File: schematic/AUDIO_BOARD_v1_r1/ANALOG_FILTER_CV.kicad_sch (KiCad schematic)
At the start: 23 parts, among them U4 LM13700, U5 OPA1678, U6 4053, U7 DAC8565, U8 LM13700

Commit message: render!
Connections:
- net at R21.2, R23.1, U5.2 (-): now also R20.2
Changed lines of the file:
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@@
+		)
+	)
+	(wire
+		(pts
+			(xy 55.88 124.46) (xy 55.88 139.7)
+		)
+		(stroke
+			(width 0)
+			(type default)
 		)
 	)

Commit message: more audio board placement
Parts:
- added C90, C91, C92, C93, C94, C95: 100nF, Capacitor_SMD:C_0402_1005Metric, symbol Device:C_Small
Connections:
- net +5V: now also C90.1, C92.1, C94.1
- net -5V: now also C91.1, C93.1, C95.1
- net GND: now also C90.2, C91.2, C92.2, C93.2, C94.2, C95.2
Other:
- note added: "DECOUPLING 100nF/IC (U4/U8/U5/U6 rails +/-5V ; U7 DAC +5V)"

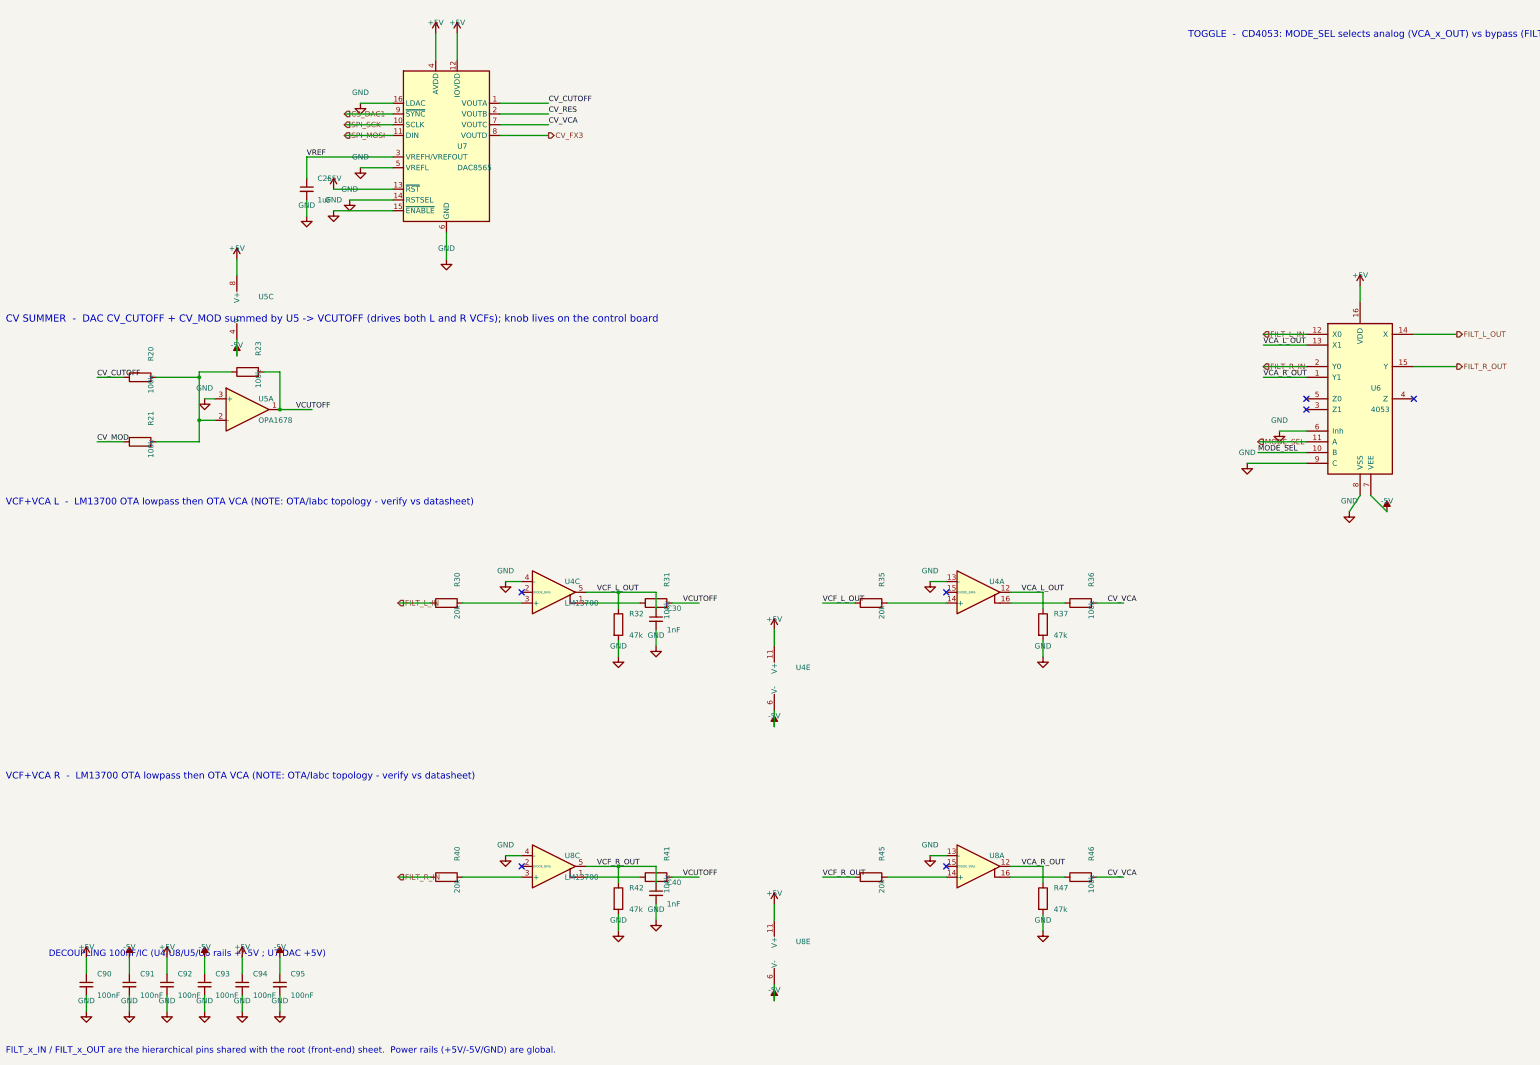
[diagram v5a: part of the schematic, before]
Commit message: placement. start with each sheet for the most part
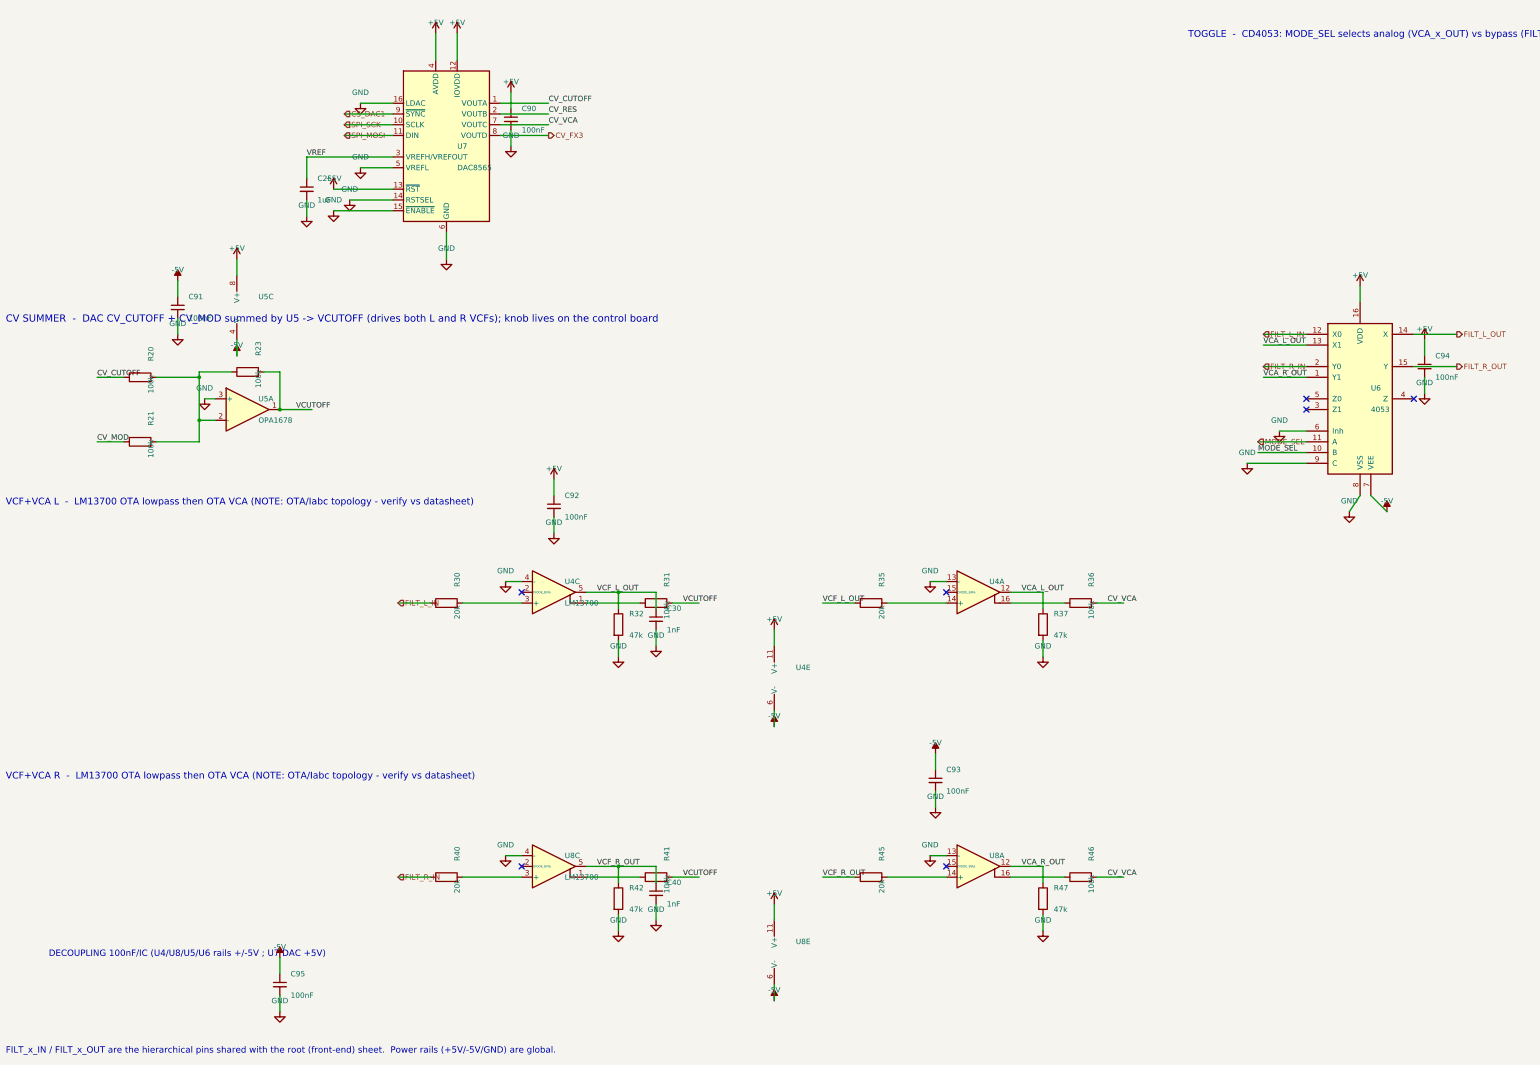
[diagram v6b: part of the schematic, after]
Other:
- moved on the sheet: C90, C91, C92, C93, C94

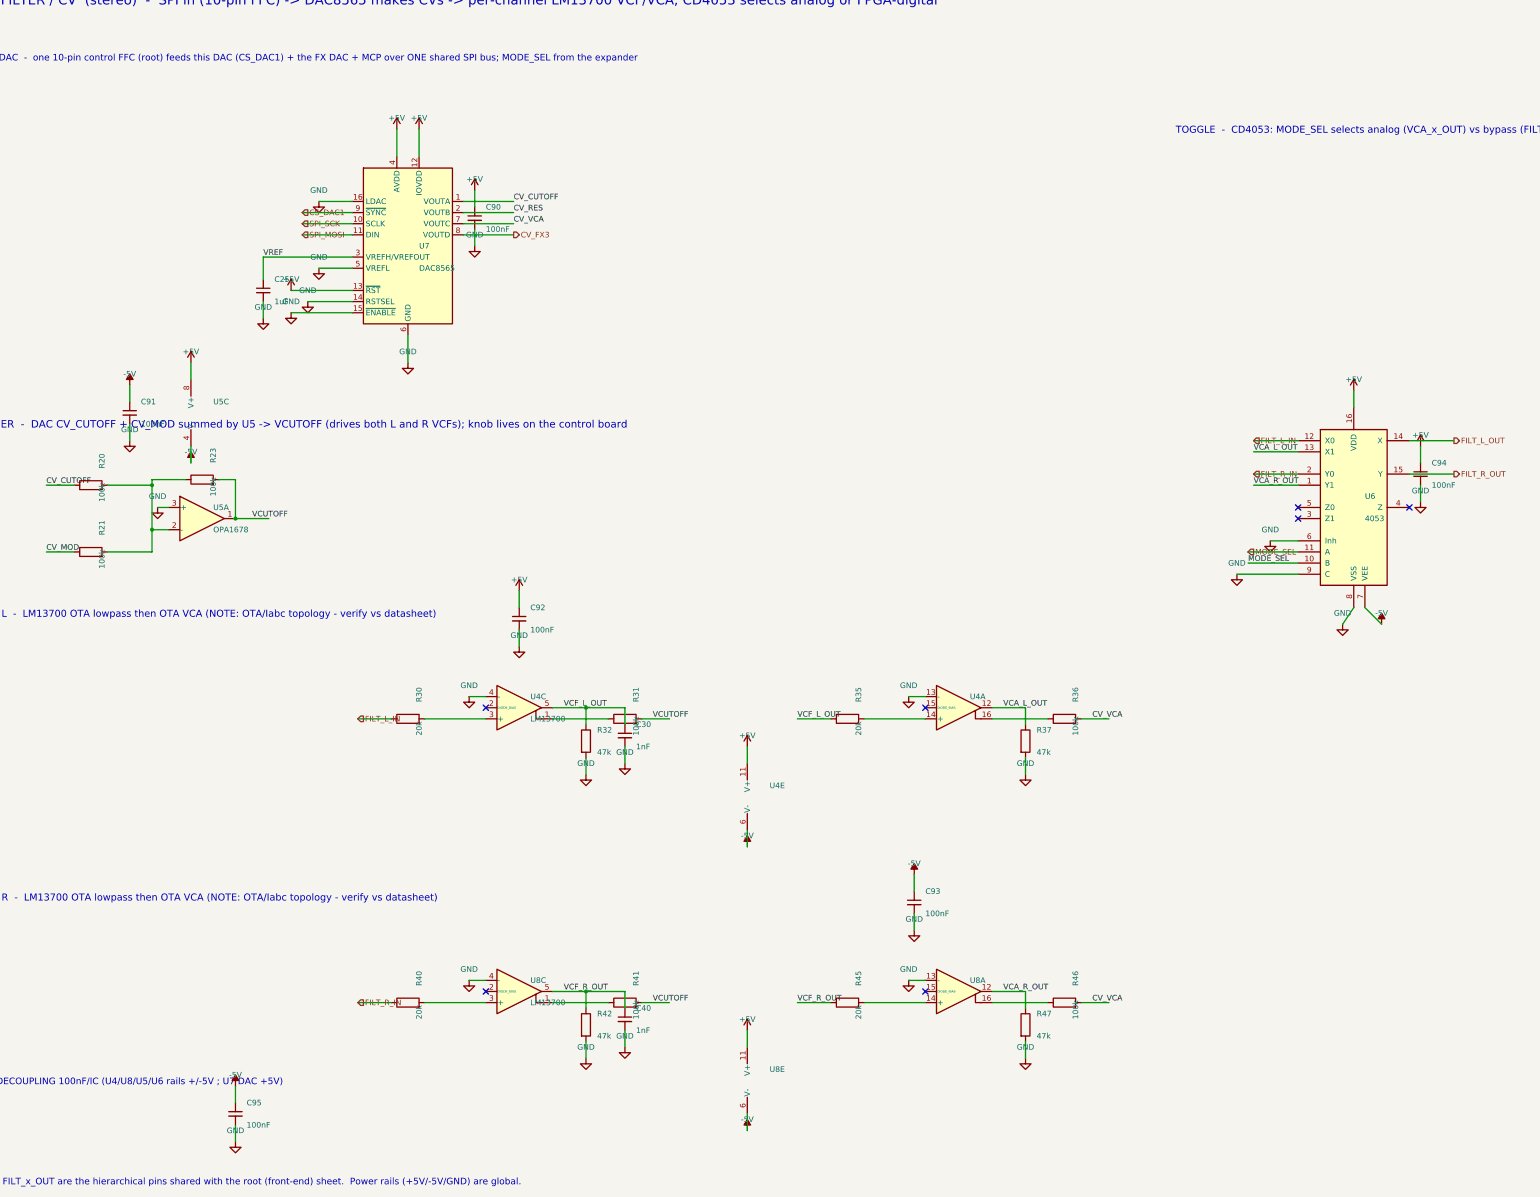
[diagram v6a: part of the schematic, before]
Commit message: more routing. more placement
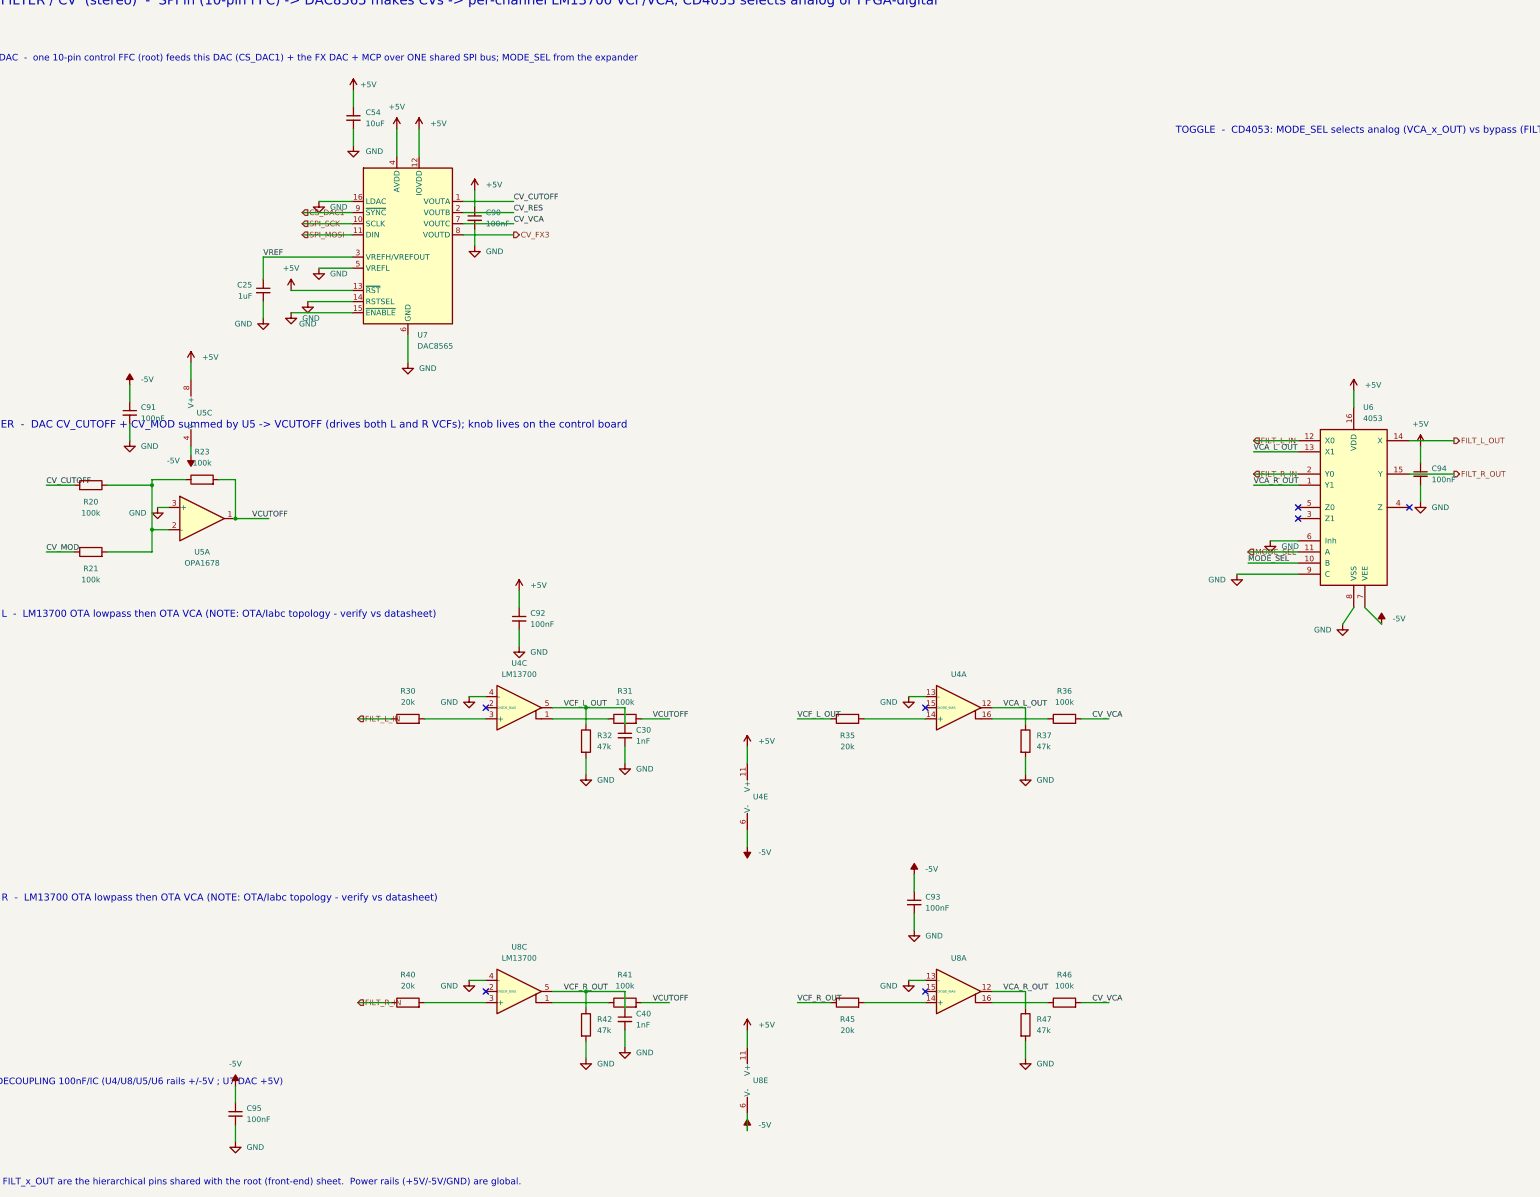
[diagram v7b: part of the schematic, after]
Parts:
- added C54: 10uF, Capacitor_SMD:C_0805_2012Metric, symbol Device:C_Small
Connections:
- net +5V: now also C54.1
- net CV_CUTOFF: now also R20.2; no longer R20.1
- net GND: now also C54.2
- net at R21.2, R23.1, U5.2 (-): now also R20.1; no longer R20.2
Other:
- moved on the sheet: R20

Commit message: try autorouter?
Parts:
- U5: footprint Package_DIP:DIP-8_W7.62mm_SMDSocket_SmallPads -> Package_SO:SOIC-8_3.9x4.9mm_P1.27mm
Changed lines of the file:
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@@
 			)
 		)
-		(property "Footprint" "Package_DIP:DIP-8_W7.62mm_SMDSocket_SmallPads"
+		(property "Footprint" "Package_SO:SOIC-8_3.9x4.9mm_P1.27mm"
 			(at 77.47 132.08 0)
 			(hide yes)
